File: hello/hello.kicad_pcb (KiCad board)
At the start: 2 copper layers, 12 parts, among them J1 pwm, J2 voltmeter, J3 common, J4 continuous, J5 common, SW1 SW_SPST, U1 Arduino nano, U2 oled i2c, U3 Rotary Encoder

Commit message: updates to final pcb design
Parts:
- moved U1 0.37 mm to (142.4, 94.9)
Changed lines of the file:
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@@
 		(tags "Through hole socket strip THT 1x01 1.27mm single row")
 		(property "Reference" "J4"
-			(at 0 -2.135 360)
+			(at 0 -2.135 0)
 			(layer "F.SilkS")
 			(effects
@@
 		)
 		(property "Value" "continuous"
-			(at 0 2.135 360)
+			(at 0 2.135 0)
 			(layer "F.Fab")
 			(effects
@@
 		)
 		(fp_text user "${REFERENCE}"
-			(at 0 0 360)
+			(at 0 0 0)
 			(layer "F.Fab")
 			(effects
@@
 		(tags "Through hole socket strip THT 1x01 1.27mm single row")
 		(property "Reference" "J2"
-			(at 0 -2.135 360)
+			(at 0 -2.135 0)
 			(layer "F.SilkS")
 			(effects
@@
 		)
 		(property "Value" "voltmeter"
-			(at 0 2.135 360)
+			(at 0 2.135 0)
 			(layer "F.Fab")
 			(effects
@@
 		)
 		(fp_text user "${REFERENCE}"
-			(at 0 0 360)
+			(at 0 0 0)
 			(layer "F.Fab")
 			(effects
@@
 		(tags "Through hole socket strip THT 1x04 1.27mm single row")
 		(property "Reference" "U2"
-			(at 0 -3 360)
+			(at 0 -3 0)
 			(layer "F.SilkS")
 			(effects
@@
 		)
 		(fp_text user "${REFERENCE}"
-			(at 0 1.905 360)
+			(at 0 1.905 0)
 			(layer "F.Fab")
 			(effects
@@
 		(tags "Through hole socket strip THT 1x05 1.27mm single row")
 		(property "Reference" "U3"
-			(at 0 -2.69 360)
+			(at 0 -2.69 0)
 			(layer "F.SilkS")
 			(effects
@@
 		)
 		(fp_text user "${REFERENCE}"
-			(at 0 2.54 360)
+			(at 0 2.54 0)
 			(layer "F.Fab")
 			(effects
@@
 		(tags "Through hole socket strip THT 1x01 1.27mm single row")
 		(property "Reference" "J5"
-			(at 0 -2.135 360)
+			(at 0 -2.135 0)
 			(layer "F.SilkS")
 			(effects
@@
 		)
 		(property "Value" "common"
-			(at 0 2.135 360)
+			(at 0 2.135 0)
 			(layer "F.Fab")
 			(effects
@@
 		)
 		(fp_text user "${REFERENCE}"
-			(at 0 0 360)
+			(at 0 0 0)
 			(layer "F.Fab")
 			(effects
@@
 		(tags "Resistor Axial_DIN0204 series Axial Vertical pin pitch 1.9mm 0.167W length 3.6mm diameter 1.6mm")
 		(property "Reference" "R1"
-			(at 0.95 -1.92 360)
+			(at 0.95 -1.92 0)
 			(layer "F.SilkS")
 			(effects
@@
 		)
 		(property "Value" "1k"
-			(at 0.95 1.92 360)
+			(at 0.95 1.92 0)
 			(layer "F.Fab")
 			(effects
@@
 		)
 		(fp_text user "${REFERENCE}"
-			(at 0.95 -1.92 360)
+			(at 0.95 -1.92 0)
 			(layer "F.Fab")
 			(effects
@@
 	(footprint "MCU_arduino_nano:Arduino_nano"
 		(layer "F.Cu")
-		(at 142.25 95.192 -90)
+		(at 142.384 94.852 -90)
 		(property "Reference" "U1"
 			(at 0.0575 -11.8295 0)
@@
 			(pinfunction "VIN")
 			(pintype "input")
+		)
+		(model "C:/Users/arnav/Downloads/Arduino_Nano.STEP"
+			(offset
+				(xyz -20 -9 0)
+			)
+			(scale
+				(xyz 1 1 1)
+			)
+			(rotate
+				(xyz 90 180 180)
+			)
 		)
 	)
@@
 		(tags "Through hole socket strip THT 1x02 1.27mm single row")
 		(property "Reference" "R2"
-			(at -0.27 -2.75 360)
+			(at -0.27 -2.75 0)
 			(layer "F.SilkS")
 			(effects
@@
 		)
 		(fp_text user "${REFERENCE}"
-			(at 0 0.635 360)
+			(at 0 0.635 0)
 			(layer "F.Fab")
 			(effects
@@
 		(tags "Through hole socket strip THT 1x01 1.27mm single row")
 		(property "Reference" "J3"
-			(at 0 -2.135 360)
+			(at 0 -2.135 0)
 			(layer "F.SilkS")
 			(effects
@@
 		)
 		(property "Value" "common"
-			(at 0 2.135 360)
+			(at 0 2.135 0)
 			(layer "F.Fab")
 			(effects
@@
 		)
 		(fp_text user "${REFERENCE}"
-			(at 0 0 360)
+			(at 0 0 0)
 			(layer "F.Fab")
 			(effects
@@
 		(tags "Through hole socket strip THT 1x01 1.27mm single row")
 		(property "Reference" "J1"
-			(at 0 -2.135 360)
+			(at 0 -2.135 0)
 			(layer "F.SilkS")
 			(effects
@@
 		)
 		(property "Value" "pwm"
-			(at 0 2.135 360)
+			(at 0 2.135 0)
 			(layer "F.Fab")
 			(effects
@@
 		)
 		(fp_text user "${REFERENCE}"
-			(at 0 0 360)
-			(layer "F.Fab")
-			(effects
+			(at 0 0 0)
+			(layer "F.Fab")
+			(effects

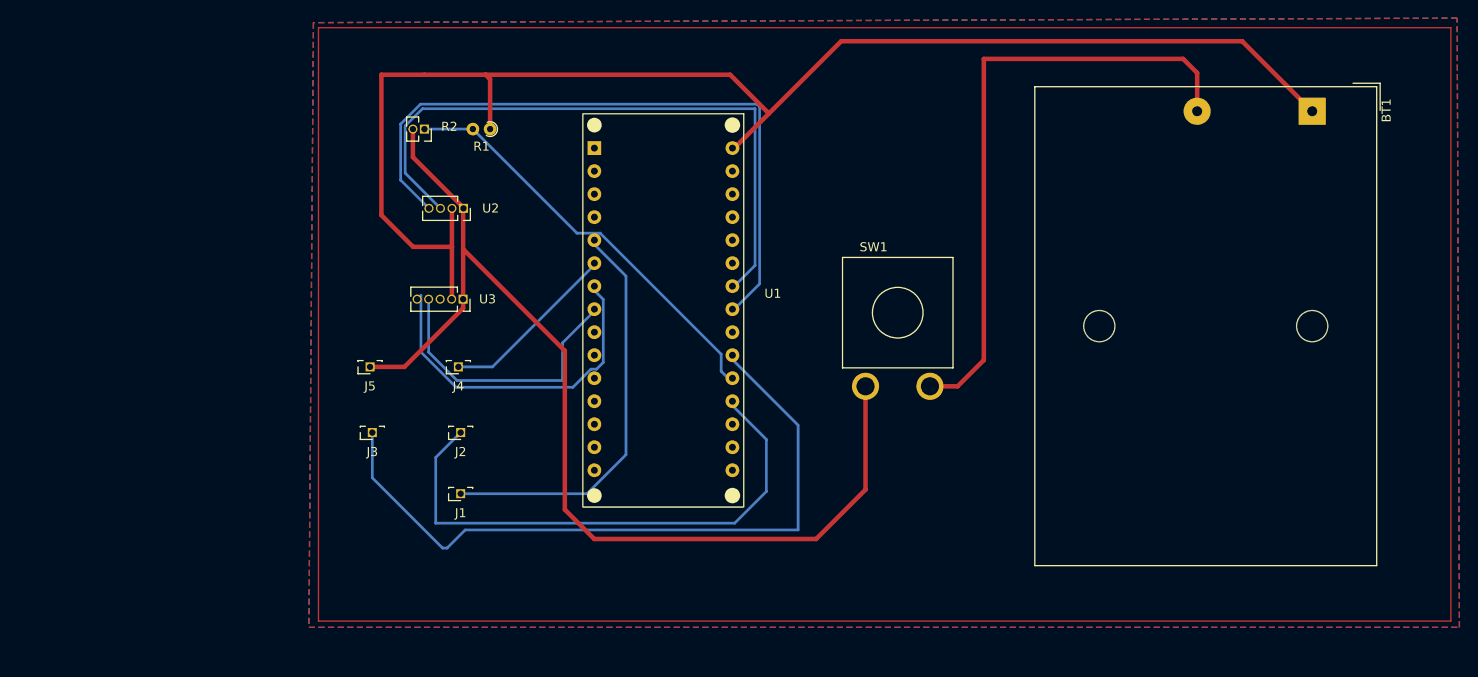
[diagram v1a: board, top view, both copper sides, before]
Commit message: revision to pcb layout
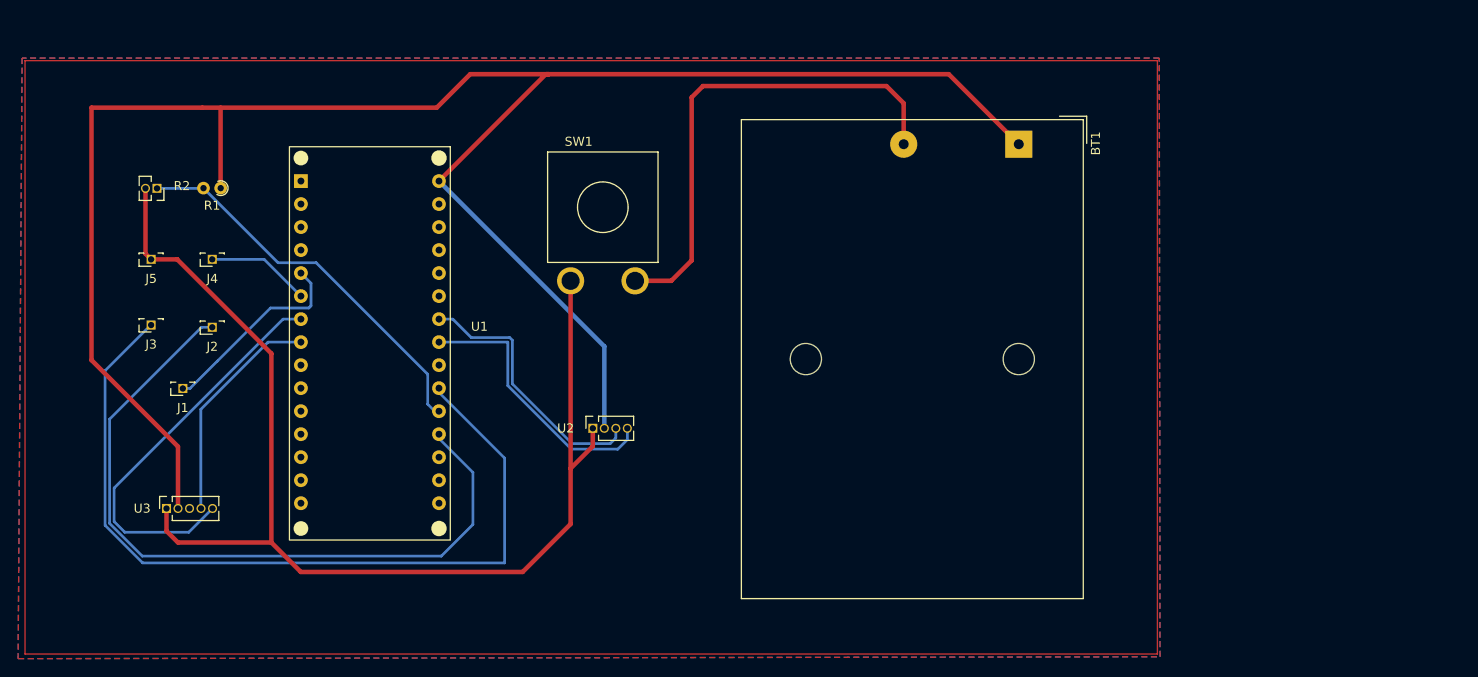
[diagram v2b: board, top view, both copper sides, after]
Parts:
- moved U3 40.1 mm to (87.3, 118.6), turned to 90 degrees
- moved SW1 34.6 mm to (135.4, 85.4)
- moved J1 32.8 mm to (89.1, 105.4)
- moved BT1 32.6 mm to (181.4, 78.4)
- moved U1 32.6 mm to (110.0, 98.5)
- moved R1 30.4 mm to (93.3, 83.3)
- moved R2 30.2 mm to (86.2, 83.3)
- moved J2 29.8 mm to (92.3, 98.6)
- moved J4 29.6 mm to (92.3, 91.1)
- moved U2 28.2 mm to (134.3, 109.8), turned to 90 degrees
- moved J3 27.2 mm to (85.6, 98.4)
- moved J5 26.9 mm to (85.6, 91.1)
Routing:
- net +5V: track 157.9 -> 216.3 mm
- net SDA: track 75.2 -> 30.2 mm
- net SCL: track 71.1 -> 29.4 mm
- net pwm: track 44.9 -> 22.0 mm
- net volt: track 60.3 -> 81.3 mm
- net /switch: track 68.8 -> 54.2 mm
- net common: track 78.0 -> 92.1 mm
- net GND: track 116.7 -> 130.2 mm
- net cont: track 19.5 -> 11.5 mm
- net CLK: track 38.3 -> 44.5 mm
- net DT: track 30.9 -> 25.1 mm
- net ohmmeter: track 46.5 -> 43.3 mm
